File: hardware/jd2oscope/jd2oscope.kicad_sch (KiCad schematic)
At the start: 4 parts, among them U1 ESP32-DEVKITC-32D

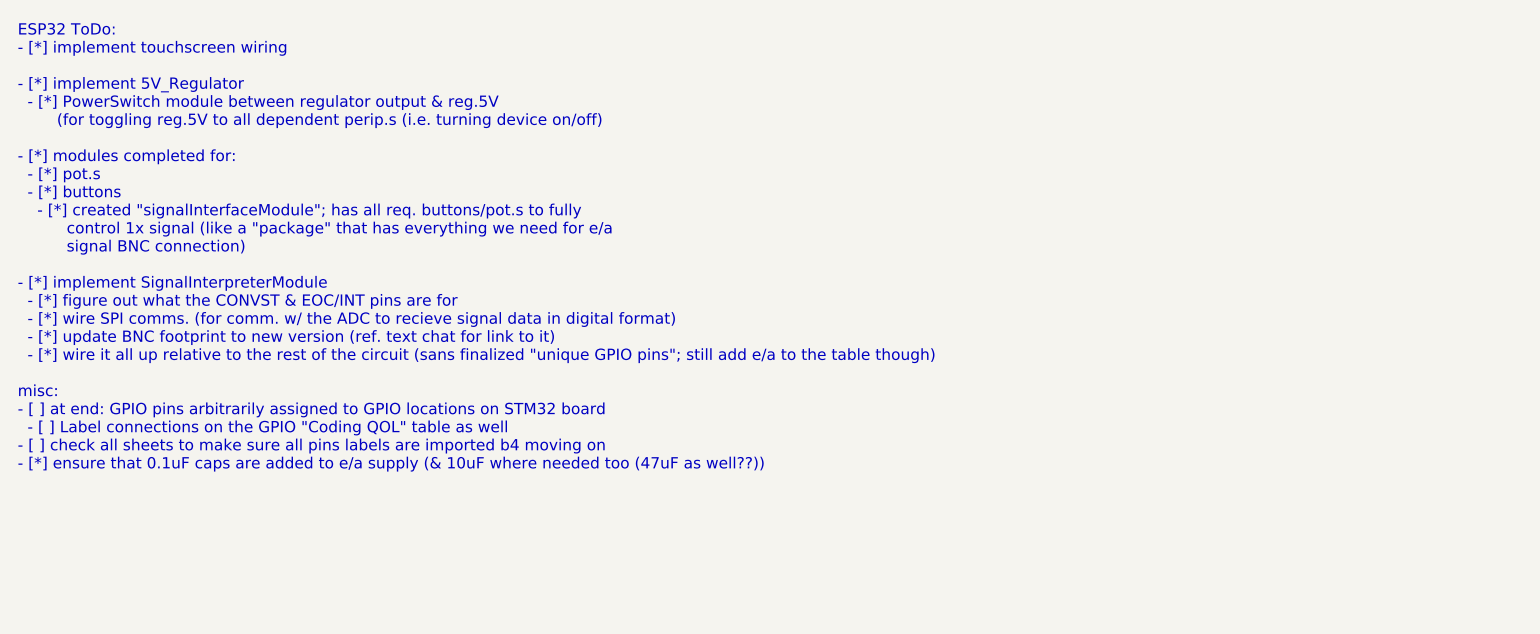
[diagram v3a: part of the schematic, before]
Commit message: feat:net lists & net classes implemented
labeled e/a net w/ net labels to clarify nodes, & created net classes w/ desired dimensions for traces; next up is assigning net classes to e/a net & using it to create the pcb!
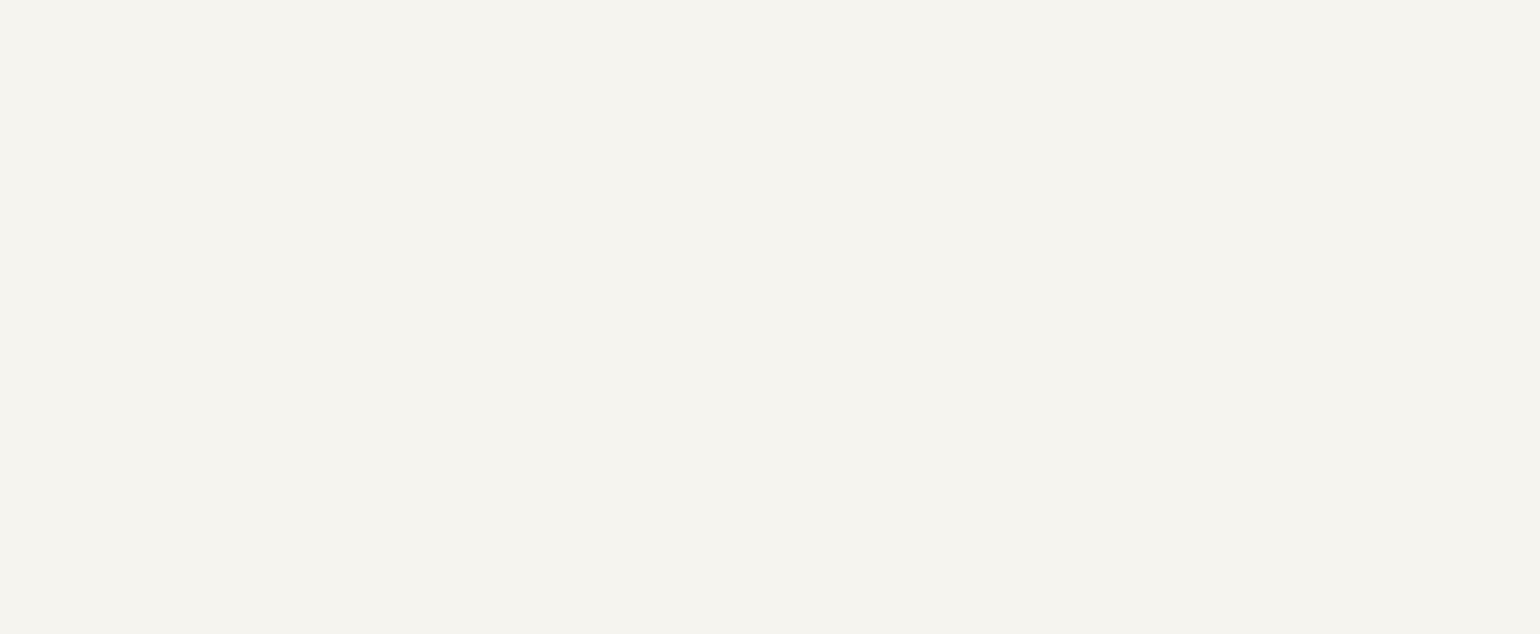
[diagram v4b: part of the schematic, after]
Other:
- note removed: "ESP32 ToDo: - [*] implement touchscreen wiring - [*] implement 5V_Regulator - [*] PowerSwitch module between regulator output & reg.5V (for toggling reg.5V to all dependent perip.s (i.e. turning device on/off) - [*] modules completed for: - [*] pot.s - [*] buttons - [*] created "signalInterfaceModule"; has all req. buttons/pot.s to fully control 1x signal (like a "package" that has everything we 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"
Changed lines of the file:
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@@
-		)
-	)
-	(text "ESP32 ToDo:\n- [*] implement touchscreen wiring\n\n- [*] implement 5V_Regulator\n  - [*] PowerSwitch module between regulator output & reg.5V\n        (for toggling reg.5V to all dependent perip.s (i.e. turning device on/off)\n\n- [*] modules completed for:\n  - [*] pot.s\n  - [*] buttons\n    - [*] created \"signalInterfaceModule\"; has all req. buttons/pot.s to fully\n          control 1x signal (like a \"package\" that has everything we need for e/a\n          signal BNC connection)\n\n- [*] implement SignalInterpreterModule\n  - [*] figure out what the CONVST & EOC/INT pins are for\n  - [*] wire SPI comms. (for comm. w/ the ADC to recieve signal data in digital format)\n  - [*] update BNC footprint to new version (ref. text chat for link to it)\n  - [*] wire it all up relative to the rest of the circuit (sans finalized \"unique GPIO pins\"; still add e/a to the table though)\n\nmisc:\n- [ ] at end: GPIO pins arbitrarily assigned to GPIO locations on STM32 board\n  - [ ] Label connections on the GPIO \"Coding QOL\" table as well\n- [ ] check all sheets to make sure all pins labels are imported b4 moving on\n- [*] ensure that 0.1uF caps are added to e/a supply (& 10uF where needed too (47uF as well??))"
-		(exclude_from_sim no)
-		(at -1.016 -27.686 0)
-		(effects
-			(font
-				(size 1.27 1.27)
-			)
-			(justify left)
 		)
 	)
